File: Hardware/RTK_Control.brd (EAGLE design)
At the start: 151.8 x 101.6 mm, 386 parts, among them J3 MICRO-SD-PUSH-PUSH-EXT-PIN, J4 Vertical Qwiic Connector, J9 MAGJACK-POE, U1 ESP32-WROVER-IE, U10 POE_PSU-DP990X, U11 MCP6021T, U12 AP7361C-33, U13 MCP6021T, U14 BP2G1+_POWER_SPLITTER, U15 USB251XB, U16 SN74AVC4T774PW, U2 CH340C, U3 XC6222B331MR-G, U4 U-BLOX_ZED-F9P, U5 U-BLOX_NEO-D9S-00B, U6 XC6222B331MR-G, U7 W5500, U8 LARA-R6001, U9 74LVC4066D_QUAD_BILATERAL_SWI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, Y1 25MHz, Y2 24MHz

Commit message: Updates after airwire review
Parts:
- removed R52: 10k, SparkFun-Resistors:0603
- removed U$115: (no value), output:#3V3_SW#0
- removed U$116: (no value), output:#SDA#7
- removed U$117: (no value), output:#SCL#8
- removed U$121: (no value), output:#TP#0
- removed U$122: (no value), output:#TP#1
- removed U$123: (no value), output:#GND#6
- removed U$63: (no value), output:VIN1
- added U$17, U$65: (no value), output:3V3_SW20
- added U$19: (no value), output:12_#_SDA20
- added U$20: (no value), output:15_#_SCL213
- added U$22, U$23: (no value), output:3V3_SW3
- added U$25, U$26: (no value), output:21_#_SDA4
- added U$28, U$30: (no value), output:22_#_SCL22
- added U$31, U$32: (no value), output:ZED_RX223
- added U$33, U$36: (no value), output:ZED_TX2224
- added U$37, U$38: (no value), output:ZED_EXTINT2225
- added U$39, U$40: (no value), output:ZED_TP2226
- added U$48: (no value), output:#I�C#0
- added U$57, U$66: (no value), output:2_#_LED0
- added U$64: (no value), output:36_#_SD_DET0
- D3: value PESD0402-0402 -> PESD0402
- U$11: device output:#3V3_SW#0 -> output:VIN#0
- U$13: device output:#GND#6 -> output:VIN#0
- U$14: device output:#ZED_RX2#0 -> output:VIN#1
- U$15: device output:#SCL#8 -> output:VIN#1
- U$16: device output:#SDA#7 -> output:GND2
- U$18: device output:#ZED_TX2#0 -> output:GND2
- U$2: device output:RESET0 -> output:4_#_#SD_CS#0
- VID2: value 10k -> 1k
- moved U$2 50.8 mm to (50.8, 10.4), flipped to the bottom, turned to 270 degrees
- moved C55 23.0 mm to (39.4, 86.7), turned to 180 degrees
- moved C52 23.0 mm to (39.4, 88.4), turned to 180 degrees
- moved POCI 20.1 mm to (41.9, 15.2)
- moved U$18 17.6 mm to (38.2, 90.9), flipped to the bottom, turned to 270 degrees
- moved U$14 17.5 mm to (34.8, 90.9)
- moved SCK 16.6 mm to (44.5, 15.2)
- moved U$101 14.1 mm to (41.9, 10.9), turned to 270 degrees
- moved U$15 14.0 mm to (34.8, 90.7), flipped to the bottom, turned to 270 degrees
- moved PICO 12.0 mm to (48.3, 15.2)
- moved U$102 11.2 mm to (44.5, 11.3), turned to 270 degrees
- moved U$11 10.7 mm to (31.2, 90.9)
- moved SD_CS 8.52 mm to (50.8, 15.2)
- moved U$13 7.27 mm to (31.2, 90.8), flipped to the bottom, turned to 270 degrees
- moved U$16 7.27 mm to (38.2, 91.1)
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- renumbered R50 to VID1, R51 to VID2, U$73 to U17
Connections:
- net DET renamed ESP36/SD_DET
- net N$37 renamed ESP35/VID
- removed net LARA_RXDO: U16.13
- removed net LARA_TXDI: U16.14
- removed net N$39: R52.2, VID2.1
- net 3.3V: now also VID2.1; no longer R52.1
- net ESP13/LARA_TXDI: now also U16.14
- net ESP14/LARA_RXDO: now also U16.13
- net GND: now also U16.11
- net VCCIO: now also U16.8
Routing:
- net ANT_NEO: track 4.06 -> 4.81 mm
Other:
- outline, holes or cut-outs redrawn

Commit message: Ready for routing
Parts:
- removed U$155, U$156: (no value), output:DET0
- added ESP5: TEST-POINTPOGO_PTH, SparkFun-Connectors:1X01_NO_SILK
- added U$63, U$70: (no value), output:VIN#0
- added U$71, U$72: (no value), output:VIN#1
- moved U$153 64.9 mm to (76.2, 44.5)
- moved LOGO7 49.9 mm to (76.2, 50.8)
- moved LOGO8 49.9 mm to (72.6, 55.9)
- moved U$44 6.49 mm to (47.1, 54.1)
- moved U$106 6.44 mm to (47.0, 54.1)
- moved !SAFEBOOT_NEO! 5.68 mm to (95.2, 66.0)
- moved U$41 5.28 mm to (95.4, 60.8), turned to 90 degrees
- moved U$93 4.45 mm to (89.9, 66.2)
- moved 9% 3.59 mm to (47.0, 55.9)
- moved C12 1.27 mm to (95.9, 67.8)
- moved C58 1.27 mm to (95.9, 73.5)
- moved R64 1.27 mm to (95.9, 71.9)
- moved U$74 1.27 mm to (101.5, 70.0)
- moved GNSS_RESET 0.64 mm to (96.5, 69.8)
- moved U$152 0.51 mm to (141.0, 40.1)
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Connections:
- new net N$37: ESP5.1, U9.9
- net D+_LARA: now also R10.1; no longer R9.1
- net D-_LARA: now also R9.1; no longer R10.1
- net GND: no longer U16.11
- net VCCIO: now also U16.6

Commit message: Partially routed
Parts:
- removed U$11, U$13: (no value), output:VIN#0
- removed U$14, U$15: (no value), output:VIN#1
- added U$73, U$75: (no value), output:50
- moved U$70 48.9 mm to (28.8, 88.9)
- moved U$72 48.9 mm to (34.7, 88.9)
- moved VIN+ 48.9 mm to (30.5, 88.9)
- moved VIN- 48.9 mm to (33.0, 88.9)
- moved U$63 48.9 mm to (28.8, 88.8)
- moved U$71 48.9 mm to (34.7, 88.8)
- moved U$74 32.4 mm to (70.0, 77.6)
- moved GNSS_RESET 22.9 mm to (74.9, 77.5), turned to 0 degrees
- moved R64 21.2 mm to (74.9, 75.2)
- moved C58 21.0 mm to (74.9, 73.3), turned to 180 degrees
- moved D14 15.9 mm to (9.27, 43.8), turned to 180 degrees
- moved R17 11.0 mm to (133.0, 12.7), turned to 90 degrees
- moved U$154 10.8 mm to (81.8, 77.6)
- moved C70 8.13 mm to (116.6, 52.8)
- moved C28 6.56 mm to (63.8, 80.9), turned to 90 degrees
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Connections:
- net N$22 renamed VIN1+
- net N$66 renamed VIN1-
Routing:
- net 3.3V_SW: track 0.00 -> 463.3 mm, vias 0 -> 26
- net 3.3V_SW2: track 0.00 -> 213.2 mm, vias 0 -> 3
- net SIM_RST: track 0.00 -> 185.3 mm, vias 0 -> 2
- net VSIM: track 0.00 -> 184.5 mm, vias 0 -> 3
- net SIM_IO: track 0.00 -> 177.7 mm, vias 0 -> 2
- net SIM_CLK: track 0.00 -> 172.1 mm, vias 0 -> 2
- net V_USB_2: track 0.00 -> 147.7 mm, vias 0 -> 2
- net ESP2/LED: track 0.00 -> 141.6 mm, vias 0 -> 3
- net V_USB: track 0.00 -> 129.9 mm, vias 0 -> 2
- net ZED_TX2: track 0.00 -> 100.9 mm, vias 0 -> 2
- net ZED_RX2: track 0.00 -> 100.8 mm, vias 0 -> 2
- net ESP21/SDA: track 0.00 -> 80.4 mm, vias 0 -> 3
- net ESP22/SCL: track 0.00 -> 76.3 mm, vias 0 -> 3
- net N$12: track 0.00 -> 70.3 mm, vias 0 -> 1
- net VCCA: track 0.00 -> 69.6 mm, vias 0 -> 10
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- added copper zone on layer 1, net 3.3V

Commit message: Almost routed
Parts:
- moved VANT 42.4 mm to (63.5, 59.7)
- moved U$105 38.1 mm to (67.3, 59.7)
- moved U$49 38.1 mm to (67.4, 59.7)
- moved R14 6.10 mm to (137.0, 16.5)
- moved U$42 5.21 mm to (71.1, 36.4)
- moved U$94 5.11 mm to (70.9, 36.4)
- moved R17 4.58 mm to (130.4, 16.5)
- moved U$43 4.46 mm to (71.0, 49.9)
- moved U$12 2.84 mm to (106.7, 92.8)
- moved !SAFEBOOT_ZED! 2.84 mm to (106.7, 87.6)
- moved U$8 2.84 mm to (101.5, 87.6)
- moved R10 1.65 mm to (135.1, 30.5)
- moved R9 1.65 mm to (136.8, 30.5)
- moved R54 1.27 mm to (71.1, 39.8)
- moved ANT_DET 1.27 mm to (71.1, 38.1)
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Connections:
- net ESP13/LARA_TXDI: now also U16.12; no longer U16.14
- net ESP34/LARA_NI: now also U16.14; no longer U16.12
- net GND: now also U16.7; no longer U16.1
- net LARA_18_NI: now also U16.3; no longer U16.5
- net LARA_18_TXDI: now also U16.5; no longer U16.3
- net VCCIO: now also U16.1; no longer U16.7
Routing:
- net ESP22/SCL: track 76.3 -> 211.3 mm, vias 3 -> 7
- net ESP25/TP: track 5.33 -> 138.5 mm, vias 0 -> 5
- net ESP21/SDA: track 80.4 -> 209.5 mm, vias 3 -> 7
- net ESP4/!SD_CS!: track 3.28 -> 98.6 mm, vias 0 -> 5
- net ZED_EXTINT: track 4.94 -> 99.6 mm, vias 0 -> 2
- net ESP19/POCI: track 50.6 -> 144.6 mm, vias 1 -> 5
- net ESP18/SCK: track 46.7 -> 138.6 mm, vias 1 -> 5
- net GNSS_!RESET!: track 26.5 -> 118.3 mm, vias 1 -> 5
- net ZED_RXI: track 0.00 -> 84.0 mm, vias 0 -> 1
- net ESP23/PICO: track 45.6 -> 125.9 mm, vias 1 -> 5
- net ZED_TXO: track 0.00 -> 77.4 mm, vias 0 -> 1
- net ESP15/SCL2: track 0.00 -> 72.0 mm, vias 0 -> 4
- net ESP36/SD_DET: track 7.79 -> 78.8 mm, vias 0 -> 3
- net !RESET!: track 49.7 -> 119.2 mm, vias 2 -> 6
- net V_ANT: track 20.9 -> 89.8 mm, vias 0 -> 2
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
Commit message: Routed
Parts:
- moved C12 0.38 mm to (95.9, 72.4)
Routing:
- net V_USB_2: track 158.5 -> 243.2 mm, vias 3 -> 5
- net N$18: track 0.00 -> 64.4 mm, vias 0 -> 2
- net N$17: track 0.00 -> 64.3 mm, vias 0 -> 2
- net N$3: track 0.00 -> 55.6 mm, vias 0 -> 2
- net N$6: track 0.00 -> 54.9 mm, vias 0 -> 2
- net CH340-RXI: track 4.07 -> 52.4 mm, vias 1 -> 2
- net ESP26/LARA_ON: track 0.00 -> 45.6 mm
- net CH340-TXO: track 4.07 -> 49.6 mm, vias 1 -> 2
- net ESP34/LARA_NI: track 0.00 -> 41.8 mm
- net ESP0/!BOOT!: track 28.8 -> 67.6 mm, vias 1 -> 2
- net ESP12/SDA2: track 0.00 -> 35.5 mm
- net ESP14/LARA_RXDO: track 0.00 -> 34.1 mm, vias 0 -> 2
- net N$46: track 0.00 -> 31.2 mm, vias 0 -> 2
- net N$47: track 0.00 -> 30.1 mm, vias 0 -> 2
- net ESP13/LARA_TXDI: track 0.00 -> 29.8 mm, vias 0 -> 2
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
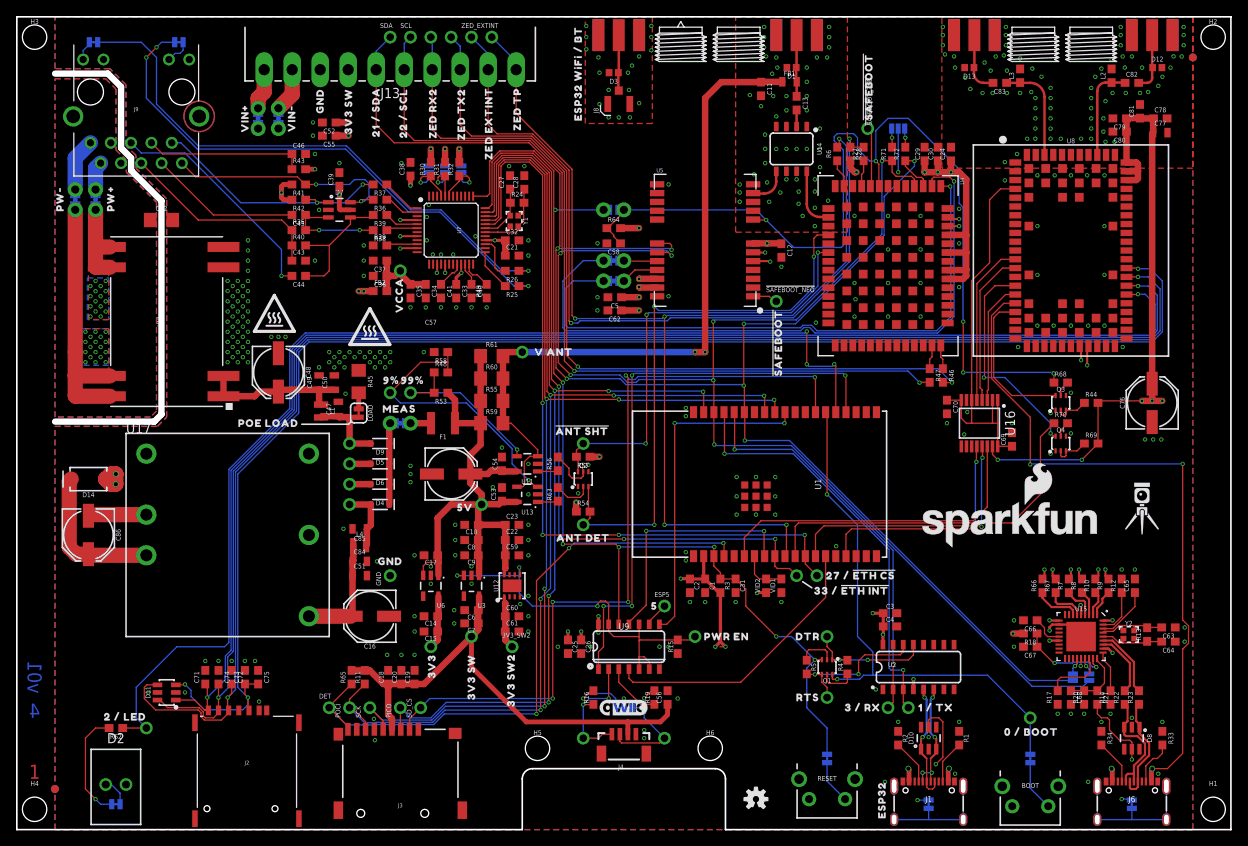
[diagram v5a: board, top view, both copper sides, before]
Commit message: Change layer 15 polygon to 3.3V_SW
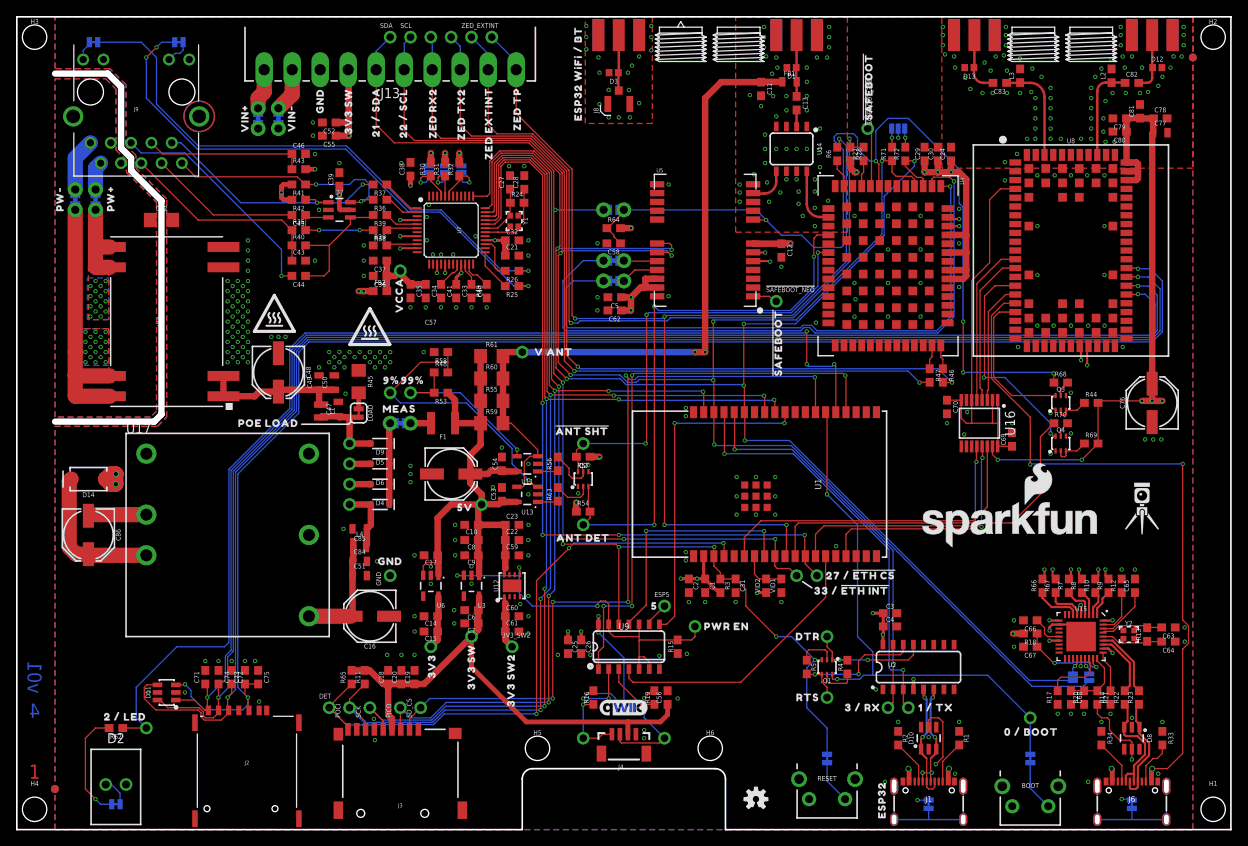
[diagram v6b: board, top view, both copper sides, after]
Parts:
- moved PWREN 1.27 mm to (85.1, 25.4)
- moved U$141 1.27 mm to (89.0, 25.4)
- moved U$59 1.27 mm to (57.1, 23.9)
- moved U$80 1.27 mm to (88.9, 25.4)
- moved U$88 1.27 mm to (57.1, 16.6)
- moved C2 0.13 mm to (84.3, 30.5)
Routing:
- net 3.3V_SW: track 476.5 -> 146.8 mm, vias 28 -> 26
- net 3.3V: track 37.5 -> 112.4 mm, vias 12 -> 10
- net V_USB: track 139.4 -> 141.6 mm
- net PWREN: track 47.9 -> 49.1 mm
- added copper zone on layer 15, net 3.3V_SW
- added copper zone on layer 15, net GND
- removed copper zone on layer 1, net 3.3V
